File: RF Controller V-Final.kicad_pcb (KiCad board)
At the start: 2 copper layers, 132 x 67.5 mm, 37 parts, among them J3 BAT+, J4 BAT-, SW1 EG1218, U1 Teensy4.0, U7 Pitch/Roll, U9 Throttle/Yaw

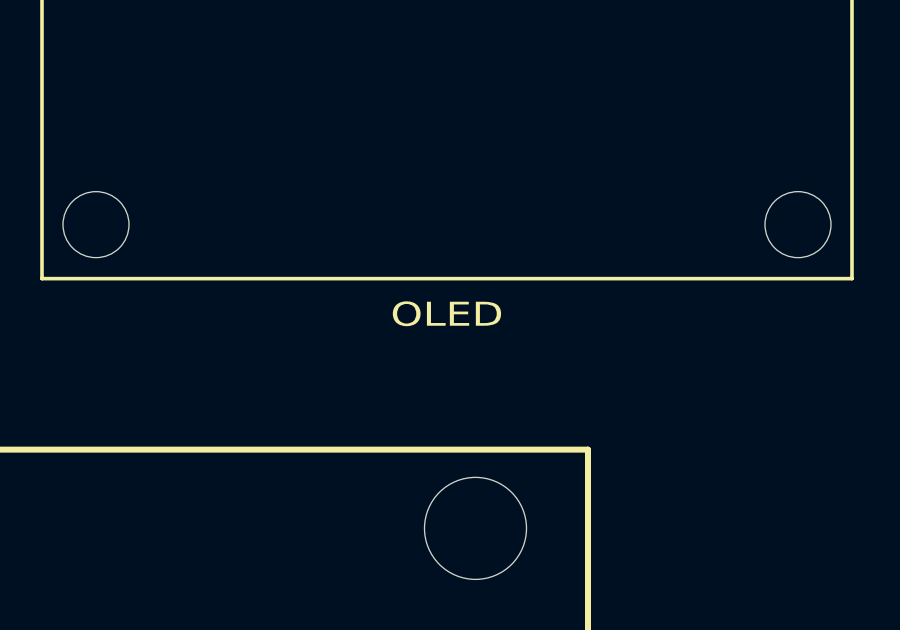
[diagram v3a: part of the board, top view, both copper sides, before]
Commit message: Add dimensions and fixed warnings
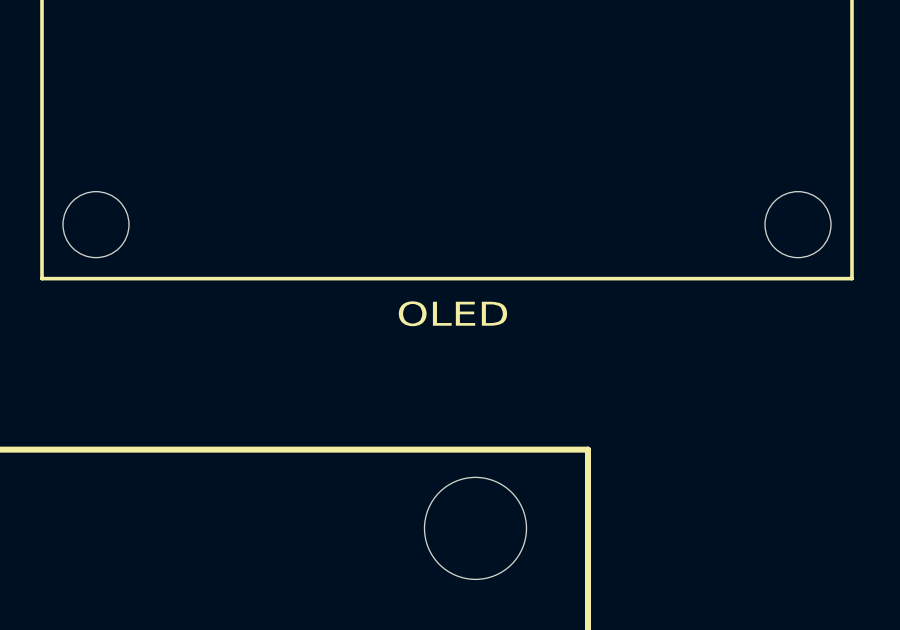
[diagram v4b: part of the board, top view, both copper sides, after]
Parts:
- renumbered OLED to J2, NRF to U3, AP to U5, TPS to U8
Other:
- board text added: "AP"
- board text added: "NRF"
- board text added: "OLED"
- board text added: "TPS"
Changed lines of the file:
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@@
 		(descr "6-pin TSOT23 package, http://cds.linear.com/docs/en/packaging/SOT_6_05-08-1636.pdf")
 		(tags "TSOT-23-6 MK06A TSOT-6 Hand-soldering")
-		(property "Reference" "TPS"
+		(property "Reference" "U8"
 			(at 0 2.5 0)
 			(layer "F.SilkS")
+			(hide yes)
 			(effects
 				(font
@@
 		(descr "Simple footprint for HiLetgo 0.96 inch SSD1306 I2C OLED 27x27mm top-header module. Header only plus module outline and reference mounting-hole circles.")
 		(tags "OLED SSD1306 I2C 128x64 0.96 HiLetgo")
-		(property "Reference" "OLED"
-			(at 3.81 26.7 0)
+		(property "Reference" "J2"
+			(at 3.51 -3.8 0)
 			(layer "F.SilkS")
+			(hide yes)
 			(effects
 				(font
@@
 		(descr "SOT, 5 Pin (JEDEC MO-178 Var AA https://www.jedec.org/document_search?search_api_views_fulltext=MO-178)")
 		(tags "SOT TO_SOT_SMD")
-		(property "Reference" "AP"
+		(property "Reference" "U5"
 			(at 0 -2.4 0)
 			(layer "F.SilkS")
+			(hide yes)
 			(effects
 				(font
@@
 		(descr "nRF24L01 breakout board")
 		(tags "nRF24L01 adapter breakout")
-		(property "Reference" "NRF"
+		(property "Reference" "U3"
 			(at 5.04 3.62 180)
 			(layer "F.SilkS")
+			(hide yes)
 			(effects
 				(font
@@
 		(layer "Edge.Cuts")
 	)
+	(gr_text "OLED"
+		(at 192.5 100.5 0)
+		(layer "F.SilkS")
+		(effects
+			(font
+				(size 0.8 1)
+				(thickness 0.15)
+			)
+		)
+	)
 	(gr_text "Teensy4.0"
 		(at 98 104 0)
@@
 		)
 	)
+	(gr_text "TPS"
+		(at 116 74 0)
+		(layer "F.SilkS")
+		(effects
+			(font
+				(size 1 1)
+				(thickness 0.15)
+			)
+		)
+	)
+	(gr_text "AP"
+		(at 138.5 71.1 0)
+		(layer "F.SilkS")
+		(effects
+			(font
+				(size 1 1)
+				(thickness 0.15)
+			)
+		)
+	)
+	(gr_text "NRF"
+		(at 163 72.5 0)
+		(layer "F.SilkS")
+		(effects
+			(font
+				(size 1 1)
+				(thickness 0.15)
+			)
+		)
+	)
+	(dimension
+		(type orthogonal)
+		(layer "Dwgs.User")
+		(pts
+			(xy 211 68) (xy 211 71)
+		)
+		(height 6)
+		(orientation 1)
+		(format
+			(prefix "")
+			(suffix "")
+			(units 3)
+			(units_format 0)
+			(precision 4)
+			(suppress_zeroes yes)
+		)
+		(style
+			(thickness 0.05)
+			(arrow_length 1.27)
+			(text_position_mode 0)
+			(arrow_direction outward)
+			(extension_height 0.58642)
+			(extension_offset 0.5)
+			(keep_text_aligned yes)
+		)
+		(gr_text "3"
+			(at 215.85 69.5 90)
+			(layer "Dwgs.User")
+			(effects
+				(font
+					(size 1 1)
+					(thickness 0.15)
+				)
+			)
+		)
+	)
+	(dimension
+		(type orthogonal)
+		(layer "Dwgs.User")
+		(pts
+			(xy 214 71) (xy 214 132.5)
+		)
+		(height 3.5)
+		(orientation 1)
+		(format
+			(prefix "")
+			(suffix "")
+			(units 3)
+			(units_format 0)
+			(precision 4)
+			(suppress_zeroes yes)
+		)
+		(style
+			(thickness 0.05)
+			(arrow_length 1.27)
+			(text_position_mode 0)
+			(arrow_direction outward)
+			(extension_height 0.58642)
+			(extension_offset 0.5)
+			(keep_text_aligned yes)
+		)
+		(gr_text "61.5"
+			(at 216.35 101.75 90)
+			(layer "Dwgs.User")
+			(effects
+				(font
+					(size 1 1)
+					(thickness 0.15)
+				)
+			)
+		)
+	)
+	(dimension
+		(type orthogonal)
+		(layer "Dwgs.User")
+		(pts
+			(xy 211 68) (xy 85 68)
+		)
+		(height -4)
+		(orientation 0)
+		(format
+			(prefix "")
+			(suffix "")
+			(units 3)
+			(units_format 0)
+			(precision 4)
+			(suppress_zeroes yes)
+		)
+		(style
+			(thickness 0.05)
+			(arrow_length 1.27)
+			(text_position_mode 0)
+			(arrow_direction outward)
+			(extension_height 0.58642)
+			(extension_offset 0.5)
+			(keep_text_aligned yes)
+		)
+		(gr_text "126"
+			(at 148 62.85 0)
+			(layer "Dwgs.User")
+			(effects
+				(font
+					(size 1 1)
+					(thickness 0.15)
+				)
+			)
+		)
+	)

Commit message: Added some art
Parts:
- added ?: LOGO, RF_MountingHoles:holeborderart, F.Cu at (210.5, 72.0)
- added ?: LOGO, RF_MountingHoles:holeborderart, F.Cu at (87.0, 131.5)
- added ?: LOGO, RF_MountingHoles:holeborderart, F.Cu at (209.5, 131.0)
- added ?: LOGO, RF_MountingHoles:holeborderart, F.Cu at (86.5, 71.5)

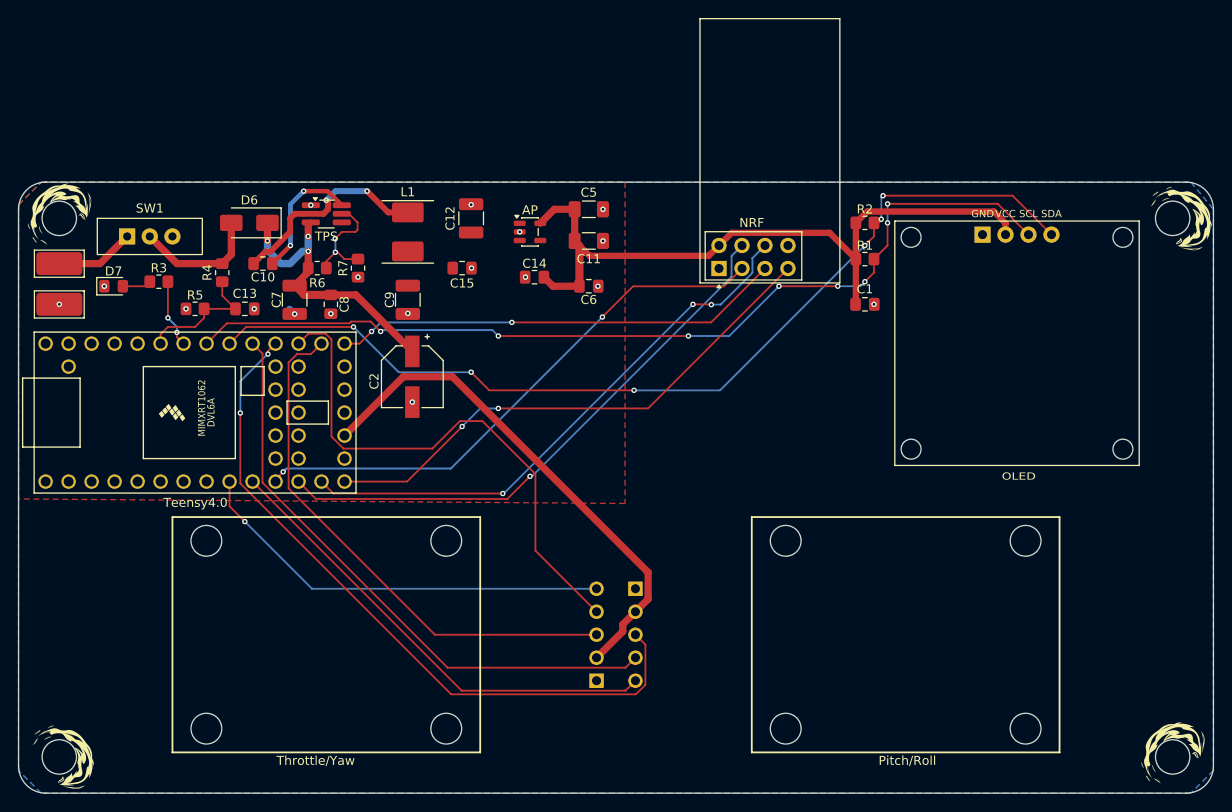
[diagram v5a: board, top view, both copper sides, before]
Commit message: Modified orientation
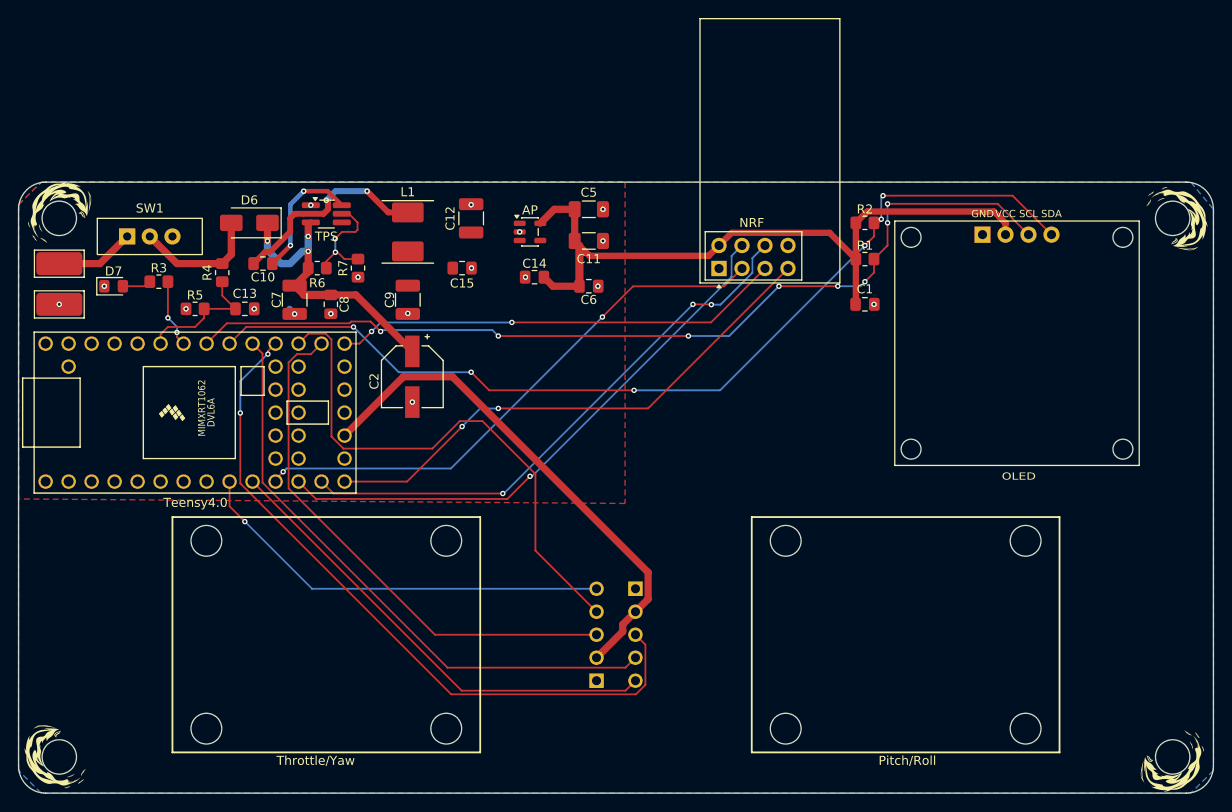
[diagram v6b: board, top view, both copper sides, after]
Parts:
- moved ? 1.00 mm to (86.0, 131.5), turned to 90 degrees
- moved ? 1.00 mm to (209.5, 132.0), turned to 180 degrees
- moved ? 0.50 mm to (210.0, 72.0)
- moved ? 0.20 mm to (86.5, 71.3)
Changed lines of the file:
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@@
 	(footprint "RF_MountingHoles:holeborderart"
 		(layer "F.Cu")
-		(at 210.5 72 -90)
+		(at 210 72 -90)
 		(property "Reference" ""
 			(at 0 0 90)
@@
 	(footprint "RF_MountingHoles:holeborderart"
 		(layer "F.Cu")
-		(at 87 131.5 -90)
+		(at 86 131.5 90)
 		(property "Reference" ""
 			(at 0 0 90)
@@
 	(footprint "RF_MountingHoles:holeborderart"
 		(layer "F.Cu")
-		(at 209.5 131)
+		(at 209.5 132 180)
 		(property "Reference" ""
 			(at 0 0 0)
@@
 	(footprint "RF_MountingHoles:holeborderart"
 		(layer "F.Cu")
-		(at 86.5 71.5)
+		(at 86.5 71.3)
 		(property "Reference" ""
 			(at 0 0 0)

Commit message: prev change was not saved
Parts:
- moved ? 0.20 mm to (86.5, 71.5)
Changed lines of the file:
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@@
 	(footprint "RF_MountingHoles:holeborderart"
 		(layer "F.Cu")
-		(at 86.5 71.3)
+		(at 86.5 71.5)
 		(property "Reference" ""
 			(at 0 0 0)

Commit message: Modified voltage reg cap and res values
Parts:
- C7: value 10u -> 22u
- R6: value 71.5k -> 47k
- R7: value 20k -> 22k
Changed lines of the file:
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@@
 			)
 		)
-		(property "Value" "10u"
+		(property "Value" "22u"
 			(at 0 2.3 90)
 			(layer "F.Fab")
@@
 			)
 		)
-		(property "Value" "20k"
+		(property "Value" "22k"
 			(at 0 1.65 90)
 			(layer "F.Fab")
@@
 			)
 		)
-		(property "Value" "71.5k"
+		(property "Value" "47k"
 			(at 0 1.65 0)
 			(layer "F.Fab")
